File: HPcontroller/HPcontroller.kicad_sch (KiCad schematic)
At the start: 14 parts

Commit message: saved more changes
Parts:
- removed D_RTD: LED, symbol Device:LED
- added D_MODE?: LED, symbol Device:LED
- added R? (x2): (no value), symbol Device:R
- added R? (x7): R, symbol Device:R
- added R?: 10k, symbol Device:R
- added SW? (x3): SW_SPST, symbol Switch:SW_SPST
- added SW?: (no value), symbol Switch:SW_SPDT
- added SW?: (no value), symbol Switch:SW_SPST
- C?: value (none) -> C
- D?: value (none) -> D
- DP_PD_POW: value (none) -> LED
- R?: value (none) -> R
- U?: value (none) -> Adafruit_QTPY_ESP32-C3
- U?: value (none) -> NCP81071B
- renumbered D_DATA_POW to D_3V3_POW
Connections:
- net GND: now also DP_PD_POW.1 (K), D_3V3_POW.1 (K), D_HEAT.1 (K), U?.3 (GND), R?.2, R?.2, R?.2, R?.2, R?.2, SW?.1 (A), SW?.2 (B), SW?.2 (B), SW?.2 (B), SW?.3 (C)
- net OUTA: now also U?.7 (OUTA)
- net OUTB: now also U?.5 (OUTB)
- net at DP_PD_POW.2 (A): now also R?.2
- net at D_MODE.1 (K): now also R?.1
- net at D_MODE.2 (A): now also U?.4 (A3)
- net FET_DRIVE: now reaches U?.1 (A0)
- net FET_DRIVE: now also U?.2 (INA), U?.4 (INB), R?.1, R?.1
- net MODE: now reaches U?.10 (MISO)
- net MODE: now also SW?.2 (B)
- net at U?.11 (MOSI): now also D_MODE?.2 (A)
- net at U?.2 (A1): now also D_HOT.2 (A)
- net at U?.3 (A2): now also D_HB.2 (A)
- net SDA: now reaches U?.5 (SDA)
- net SCL: now reaches U?.6 (SCL)
- net RUN: now reaches U?.7 (TX)
- net RUN: now also SW?.1 (A)
- net DEC: now reaches U?.8 (RX)
- net DEC: now also SW?.1 (A)
- net INC: now reaches U?.9 (SCK)
- net INC: now also SW?.1 (A)
- net at D_HB.1 (K): now also R?.1
- net at D_HEAT.2 (A): now also R?.2
- net at D_3V3_POW.2 (A): now also R?.2
- net at U?.1 (ENA): now also U?.8 (ENB), R?.2, R?.2
- net at D_HOT.1 (K): now also R?.1
- new net: D_MODE?.1 (K), R?.1
- new net +3V3: R?.1, R?.1, SW?.1 (A)
- new net ThermalProtector/THM_PROT_OUT: R?.1
- new net ThermalProtector/THM_PROT_RES: SW?.2 (B)
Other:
- added sheet ThermalProtector (ThermalProtector.kicad_sch)
- moved on the sheet: C?, D?, D_HB, D_HEAT, D_HOT, D_MODE, Q?A, Q?B, R?, U?

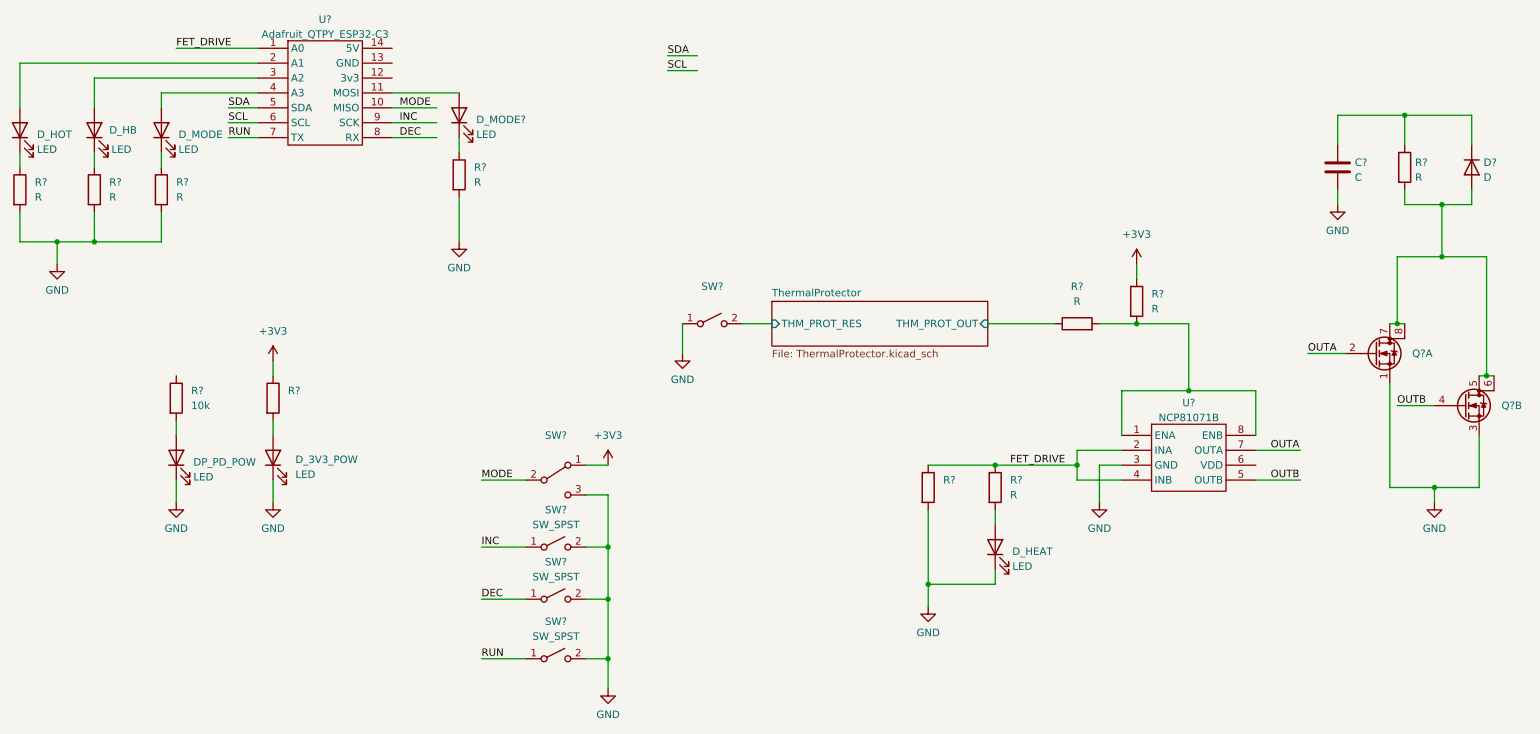
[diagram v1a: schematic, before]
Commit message: assigned footprints, added some stuff to readme
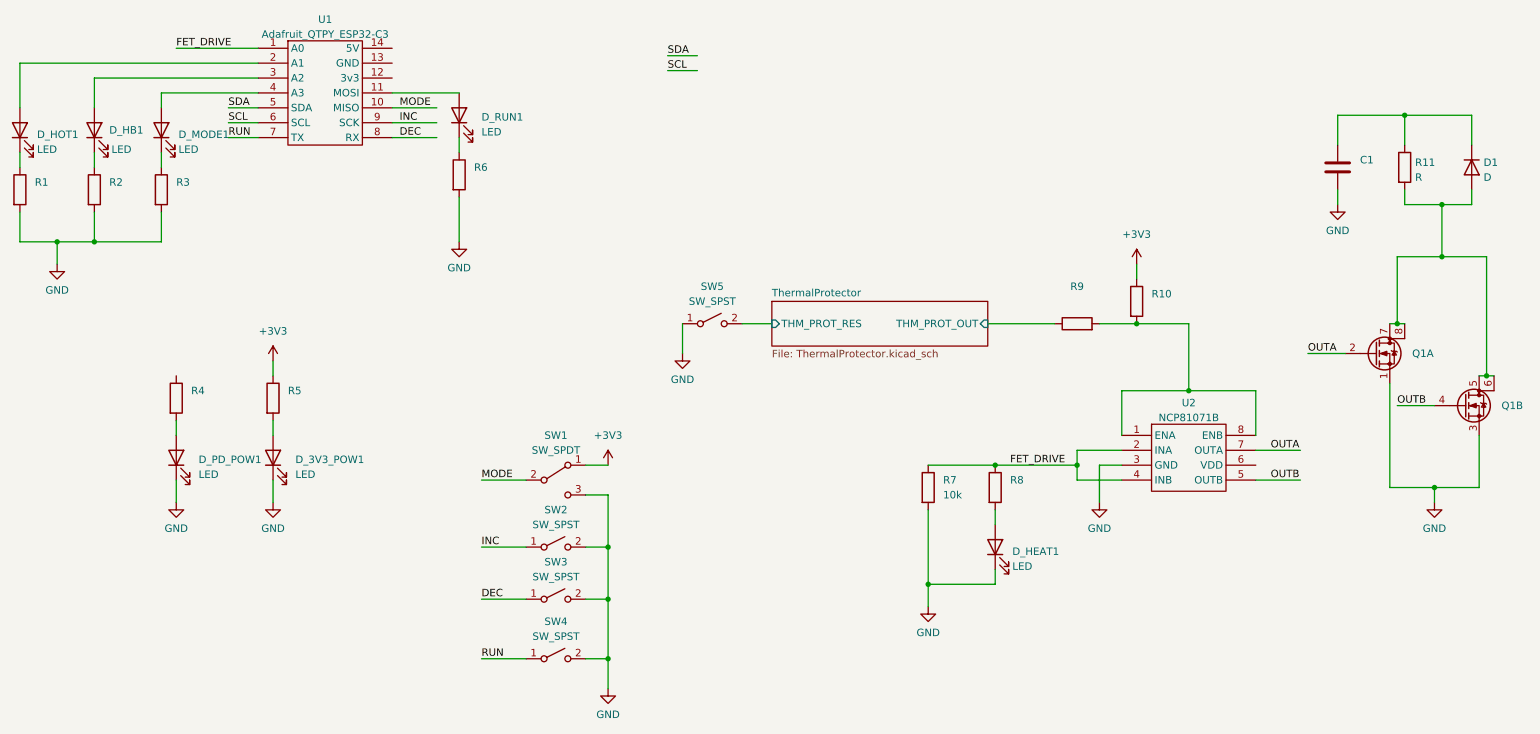
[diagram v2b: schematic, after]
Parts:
- C1: renamed from C?; value C -> (none)
- Q1: renamed from Q?; value (none) -> Q_Dual_NMOS_S1G1S2G2D2D2D1D1
- R1, R10, R2, R3, R6, R8, R9: renamed from R?; value R -> (none)
- R4: renamed from R?; value 10k -> (none)
- R7: renamed from R?; value (none) -> 10k
- SW1: renamed from SW?; value (none) -> SW_SPDT
- SW5: renamed from SW?; value (none) -> SW_SPST
- gave numbers to parts that had none: 9
- renumbered D_3V3_POW to D_3V3_POW1, D_HB to D_HB1, D_HEAT to D_HEAT1, D_HOT to D_HOT1, D_MODE to D_MODE1, DP_PD_POW to D_PD_POW1

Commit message: started layout
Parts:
- removed D_HB1, D_MODE1: LED, symbol Device:LED
- added C2, C4: (no value), symbol Device:C
- added C3: C, symbol Device:C
- added J1: (no value), symbol Connector:Screw_Terminal_01x02
- added R14: (no value), symbol Device:R
- added U4: (no value), symbol dcdcmodule:VR10S3V3
- added U5: (no value), symbol DevBoards:ER-OLED0.49-1_MODULE
- added U6: (no value), symbol DevBoards:Adafruit_MAX31850
- C1: value (none) -> 10u; footprint (none) -> Capacitor_SMD:C_0805_2012Metric_Pad1.18x1.45mm_HandSolder
- D1: footprint (none) -> Diode_SMD:D_SMB_Handsoldering
- D_3V3_POW1, D_HEAT1, D_HOT1, D_PD_POW1, D_RUN1: footprint (none) -> LED_SMD:LED_0603_1608Metric_Pad1.05x0.95mm_HandSolder
- Q1, U2: footprint (none) -> Package_SO:SOIC-8_3.9x4.9mm_P1.27mm
- R1, R5, R6, R8: value (none) -> 100; footprint (none) -> Resistor_SMD:R_0805_2012Metric_Pad1.20x1.40mm_HandSolder
- R10: value (none) -> 10k; footprint (none) -> Resistor_SMD:R_0805_2012Metric_Pad1.20x1.40mm_HandSolder
- R11, R7: footprint (none) -> Resistor_SMD:R_0805_2012Metric_Pad1.20x1.40mm_HandSolder
- R2: value (none) -> 4k7
- R4: value (none) -> 1k5; footprint (none) -> Resistor_SMD:R_0805_2012Metric_Pad1.20x1.40mm_HandSolder
- R9: value (none) -> 0; footprint (none) -> Jumper:SolderJumper-2_P1.3mm_Bridged_RoundedPad1.0x1.5mm
- SW1: footprint (none) -> Button_Switch_THT:SW_Slide_1P2T_CK_OS102011MS2Q
- SW2, SW3, SW4, SW5: footprint (none) -> Button_Switch_SMD:SW_SPST_PTS645
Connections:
- net +3V3: now also R2.1, R3.1, U1.12 (3v3), C3.1, R14.1, U4.3 (+Vout_3v3), U5.2 (VCC), U6.6 (3v3)
- net GND: now also D_HOT1.1 (K), U1.13 (GND), C2.2, C3.2, C4.2, J1.1 (Pin_1), U4.2 (GND), U5.1 (GND), U6.8 (GND); no longer R1.2, R2.2, R3.2
- net SCL: now also R2.2, U5.3 (SCL)
- net SDA: now also R3.2, U5.4 (SDA)
- net VCC: now reaches R4.1
- net VCC: now also C1.1, D1.1 (K), R11.1, U2.6 (VDD), C2.1, C4.1, J1.2 (Pin_2), U4.1 (+Vin)
- net OW_DATA: now reaches U1.4 (A3)
- net OW_DATA: now also R14.2, U6.1 (DATA)
- net at U1.2 (A1): now also R1.1; no longer D_HOT1.2 (A)
- new net: D_HOT1.2 (A), R1.2
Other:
- note added: "VCC should be 20V from USB PD"
- moved on the sheet: C1, D1, D_3V3_POW1, D_HOT1, D_PD_POW1, D_RUN1, Q1A, Q1B, R1, R10, R11, R4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
